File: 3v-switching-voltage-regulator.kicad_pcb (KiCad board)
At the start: 2 copper layers, 45.5 x 30.5 mm, 16 parts, among them J1 USB_C_Receptacle_PowerOnly_6P, U1 MP1584EN

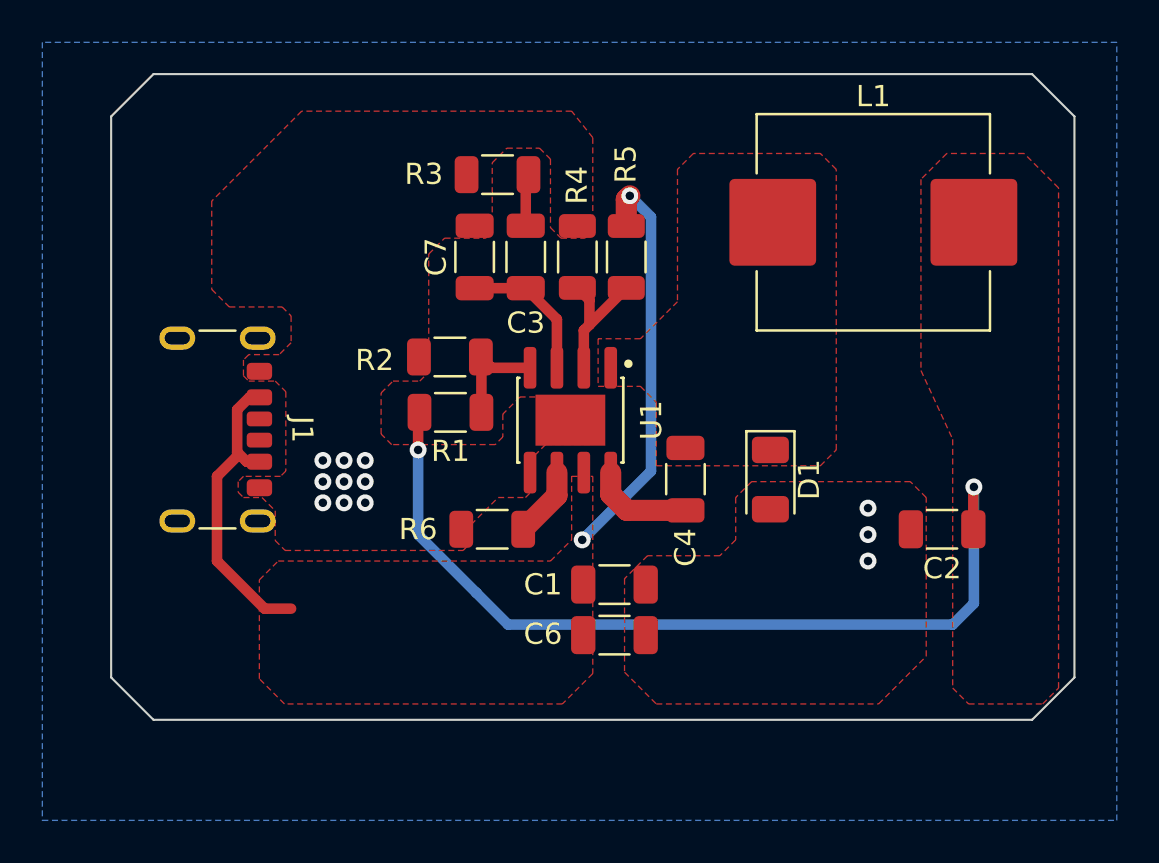
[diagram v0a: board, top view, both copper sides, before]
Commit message: reduces board size and adds input output connections
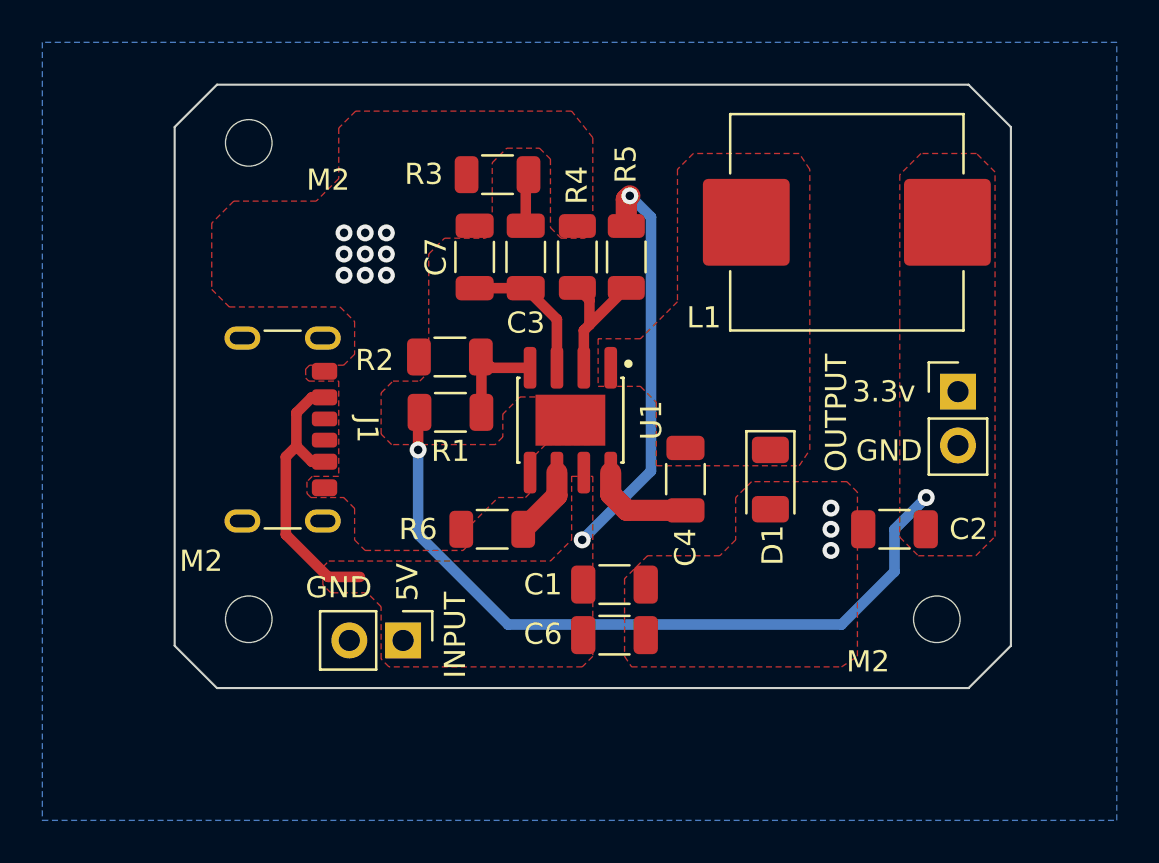
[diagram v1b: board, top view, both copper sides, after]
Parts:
- added INPUT: Conn_01x02, Connector_PinHeader_2.54mm:PinHeader_1x02_P2.54mm_Vertical, F.Cu at (91.5, 61.8)
- added J2: Conn_01x02, Connector_PinHeader_2.54mm:PinHeader_1x02_P2.54mm_Vertical, F.Cu at (117.8, 50.0)
- added M2: MountingHole_2.2mm_M2, MountingHole:MountingHole_2.2mm_M2, F.Cu at (84.2, 38.2)
- added M2: MountingHole_2.2mm_M2, MountingHole:MountingHole_2.2mm_M2, F.Cu at (84.2, 60.8)
- added M2: MountingHole_2.2mm_M2, MountingHole:MountingHole_2.2mm_M2, F.Cu at (116.8, 60.8)
- moved J1 3.08 mm to (84.8, 51.8)
- moved C2 2.25 mm to (114.8, 56.5)
- moved L1 1.25 mm to (112.5, 42.0)
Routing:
- net Vout3.3: track 41.7 -> 35.2 mm
- net VIN: track 34.0 -> 33.1 mm
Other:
- board size 45.5 x 30.5 mm -> 39.5 x 28.5 mm
- board text added: "3.3v"
- board text added: "5V"
- board text added: "GND"
- board text added: "OUTPUT"

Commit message: generats fabrication files for JLCPCB
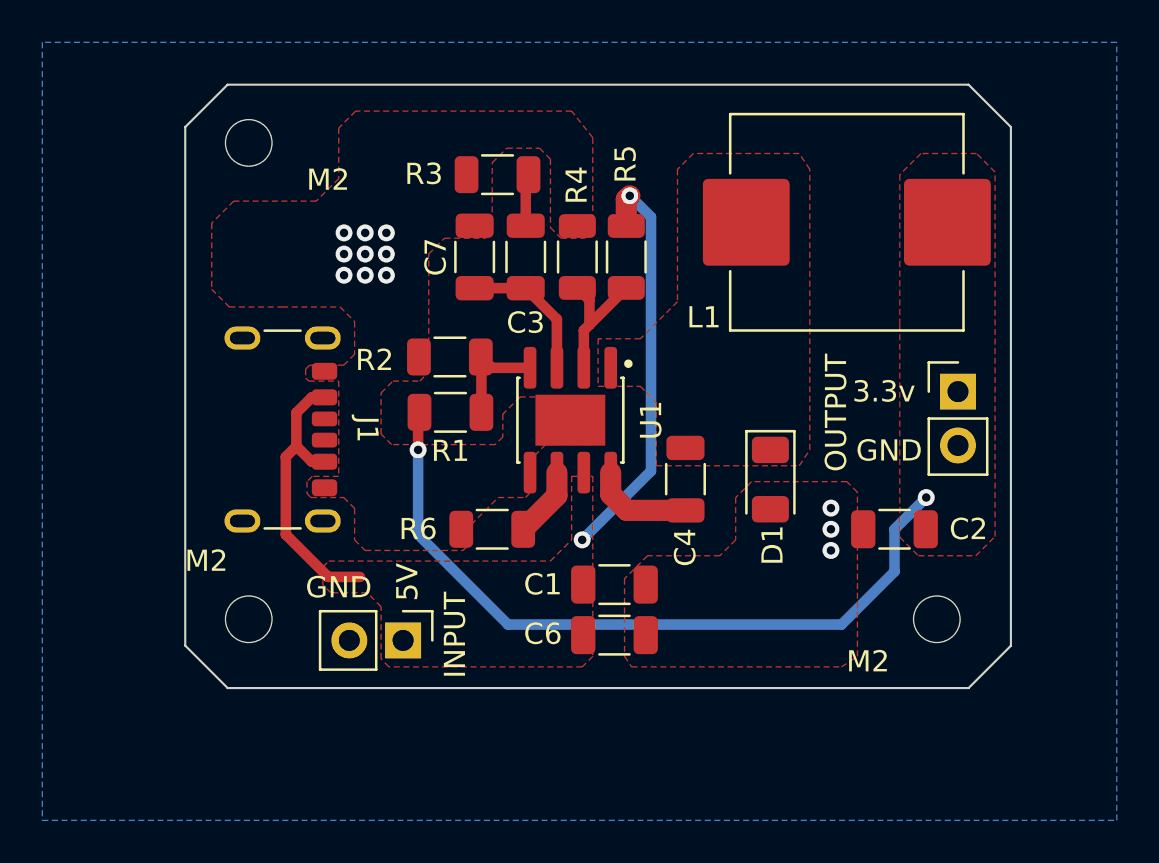
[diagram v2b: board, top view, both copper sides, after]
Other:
- board size 39.5 x 28.5 mm -> 39 x 28.5 mm
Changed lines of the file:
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@@
 			(outputformat 1)
 			(mirror no)
-			(drillshape 1)
+			(drillshape 0)
 			(scaleselection 1)
-			(outputdirectory "")
+			(outputdirectory "production/v1/")
 		)
 	)
@@
 		(tags "mountinghole M2")
 		(property "Reference" "M2"
-			(at -2.25 -2.75 0)
+			(at -2 -2.75 0)
 			(layer "F.SilkS")
 			(effects
@@
 	)
 	(gr_line
-		(start 80.75 62)
-		(end 80.75 37.5)
+		(start 81.25 62)
+		(end 81.25 37.5)
 		(stroke
 			(width 0.1)
@@
 	)
 	(gr_line
-		(start 120.25 62)
-		(end 120.25 37.5)
+		(start 83.25 35.5)
+		(end 118.25 35.5)
 		(stroke
 			(width 0.1)
@@
 	)
 	(gr_line
-		(start 82.75 64)
-		(end 80.75 62)
+		(start 83.25 64)
+		(end 81.25 62)
 		(stroke
 			(width 0.1)
@@
 	)
 	(gr_line
-		(start 118.25 35.5)
-		(end 120.25 37.5)
+		(start 81.25 37.5)
+		(end 83.25 35.5)
 		(stroke
 			(width 0.1)
@@
 	)
 	(gr_line
-		(start 118.25 64)
-		(end 82.75 64)
+		(start 120.25 37.5)
+		(end 118.25 35.5)
 		(stroke
 			(width 0.1)
@@
 	)
 	(gr_line
-		(start 82.75 35.5)
-		(end 80.75 37.5)
+		(start 83.25 64)
+		(end 118.25 64)
 		(stroke
 			(width 0.1)
@@
 	)
 	(gr_line
-		(start 118.25 35.5)
-		(end 82.75 35.5)
+		(start 120.25 62)
+		(end 120.25 37.5)
 		(stroke
 			(width 0.1)
@@
 		(polygon
 			(pts
-				(xy 116 38.75) (xy 115 39.75) (xy 115 46.833334) (xy 115 46.833334) (xy 115 56.875) (xy 115.875 57.75)
-				(xy 118.59375 57.75) (xy 119.5 56.84375) (xy 119.5 39.625) (xy 118.625 38.75)
+				(xy 116 38.75) (xy 115 39.75) (xy 115 46.833334) (xy 115 56.875) (xy 115.875 57.75) (xy 118.59375 57.75)
+				(xy 119.5 56.84375) (xy 119.5 39.625) (xy 118.625 38.75)
 			)
 		)
